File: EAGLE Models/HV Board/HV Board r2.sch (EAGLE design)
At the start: 27 parts, among them K1 HE751, U1 G2RL-1-E, U2 CNY17-3, U3 MJD45H11T4G, U4 MMBT4401-7-F

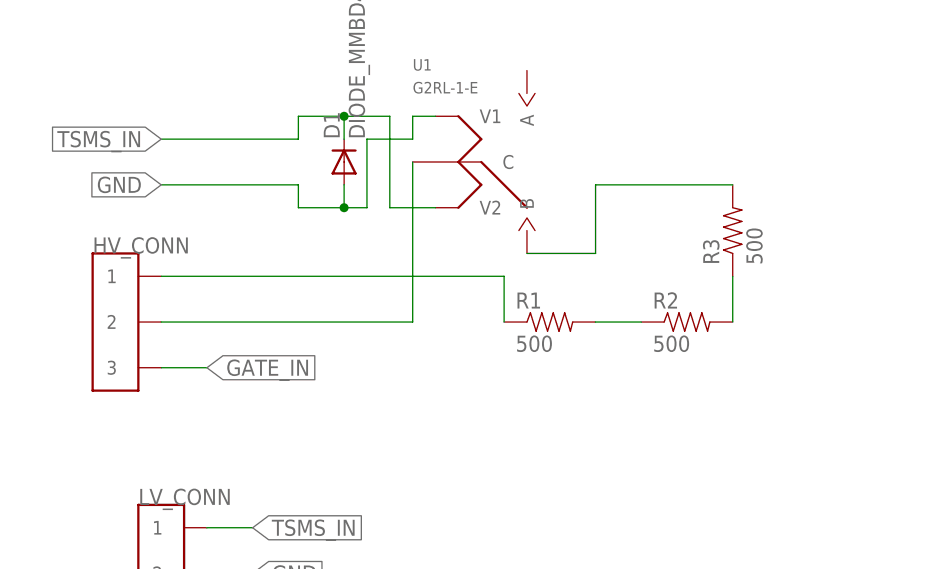
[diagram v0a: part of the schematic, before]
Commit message: Changed HV board for putting in line with MC
Integrated Discharge and TSAL circuit into one smaller board to put in a
box in line with the motor controller.
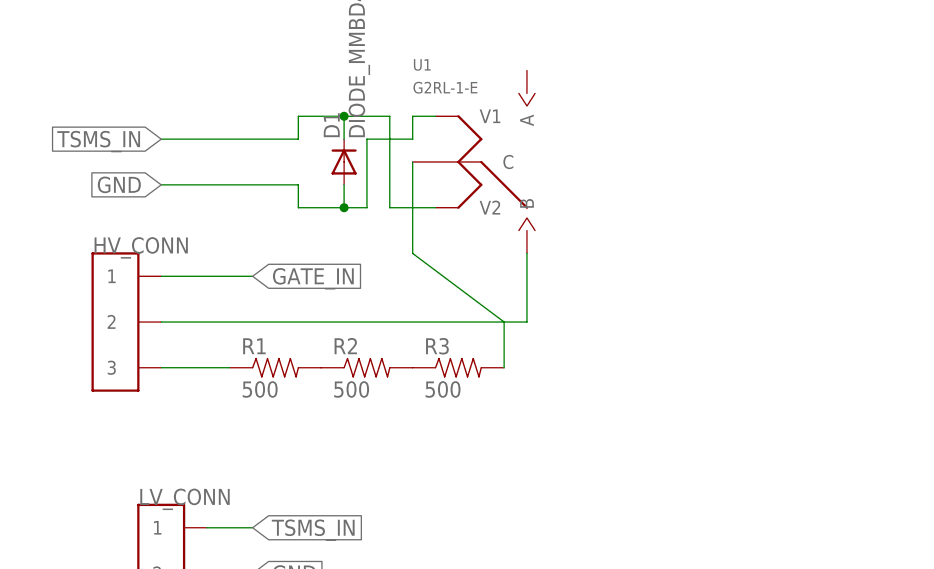
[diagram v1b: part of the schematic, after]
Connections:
- net GATE_IN: now also HV_CONN.1; no longer HV_CONN.3
- net HV+: now also U1.B; no longer U1.C
- net HV-: now also HV_CONN.3; no longer HV_CONN.1
- net N$3: now also U1.C; no longer U1.B
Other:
- moved on the sheet: R1, R2, R3
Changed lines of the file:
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@@
 <?xml version="1.0" encoding="utf-8"?>
 <!DOCTYPE eagle SYSTEM "eagle.dtd">
-<eagle version="7.1.0">
+<eagle version="7.2.0">
 <drawing>
 <settings>
@@
 <instance part="U1" gate="G$1" x="-33.02" y="-91.44"/>
 <instance part="D1" gate="G$1" x="-45.72" y="-91.44" rot="R90"/>
-<instance part="R1" gate="G$1" x="-22.86" y="-109.22"/>
-<instance part="R2" gate="G$1" x="-7.62" y="-109.22"/>
-<instance part="R3" gate="G$1" x="-2.54" y="-99.06" rot="R90"/>
+<instance part="R1" gate="G$1" x="-53.34" y="-114.3"/>
+<instance part="R2" gate="G$1" x="-43.18" y="-114.3"/>
+<instance part="R3" gate="G$1" x="-33.02" y="-114.3"/>
 <instance part="C2" gate="G$1" x="330.2" y="-104.14" smashed="yes">
 <attribute name="NAME" x="334.01" y="-105.41" size="1.778" layer="95" align="center-left"/>
@@
 <net name="N$3" class="0">
 <segment>
-<pinref part="U1" gate="G$1" pin="B"/>
-<wire x1="-25.4" y1="-101.6" x2="-17.78" y2="-101.6" width="0.1524" layer="91"/>
 <pinref part="R3" gate="G$1" pin="2"/>
-<wire x1="-2.54" y1="-93.98" x2="-17.78" y2="-93.98" width="0.1524" layer="91"/>
-<wire x1="-17.78" y1="-93.98" x2="-17.78" y2="-101.6" width="0.1524" layer="91"/>
+<wire x1="-27.94" y1="-114.3" x2="-27.94" y2="-109.22" width="0.1524" layer="91"/>
+<wire x1="-27.94" y1="-109.22" x2="-38.1" y2="-101.6" width="0.1524" layer="91"/>
+<pinref part="U1" gate="G$1" pin="C"/>
+<wire x1="-38.1" y1="-101.6" x2="-38.1" y2="-91.44" width="0.1524" layer="91"/>
 </segment>
 </net>
@@
 <pinref part="R1" gate="G$1" pin="2"/>
 <pinref part="R2" gate="G$1" pin="1"/>
-<wire x1="-17.78" y1="-109.22" x2="-12.7" y2="-109.22" width="0.1524" layer="91"/>
 </segment>
 </net>
@@
 <pinref part="R2" gate="G$1" pin="2"/>
 <pinref part="R3" gate="G$1" pin="1"/>
-<wire x1="-2.54" y1="-109.22" x2="-2.54" y2="-104.14" width="0.1524" layer="91"/>
 </segment>
 </net>
@@
 </segment>
 <segment>
-<pinref part="U1" gate="G$1" pin="C"/>
-<wire x1="-38.1" y1="-109.22" x2="-38.1" y2="-91.44" width="0.1524" layer="91"/>
 <pinref part="HV_CONN" gate="G$1" pin="2"/>
-<wire x1="-66.04" y1="-109.22" x2="-38.1" y2="-109.22" width="0.1524" layer="91"/>
+<wire x1="-25.4" y1="-109.22" x2="-66.04" y2="-109.22" width="0.1524" layer="91"/>
+<pinref part="U1" gate="G$1" pin="B"/>
+<wire x1="-25.4" y1="-109.22" x2="-25.4" y2="-101.6" width="0.1524" layer="91"/>
 </segment>
 </net>
@@
 </segment>
 <segment>
-<pinref part="HV_CONN" gate="G$1" pin="1"/>
-<wire x1="-27.94" y1="-104.14" x2="-66.04" y2="-104.14" width="0.1524" layer="91"/>
 <pinref part="R1" gate="G$1" pin="1"/>
-<wire x1="-27.94" y1="-104.14" x2="-27.94" y2="-109.22" width="0.1524" layer="91"/>
+<pinref part="HV_CONN" gate="G$1" pin="3"/>
+<wire x1="-58.42" y1="-114.3" x2="-66.04" y2="-114.3" width="0.1524" layer="91"/>
 </segment>
 <segment>
@@
 <net name="GATE_IN" class="0">
 <segment>
-<pinref part="HV_CONN" gate="G$1" pin="3"/>
-<wire x1="-66.04" y1="-114.3" x2="-60.96" y2="-114.3" width="0.1524" layer="91"/>
-<label x="-60.96" y="-114.3" size="1.778" layer="95" xref="yes"/>
-</segment>
-<segment>
+<label x="-55.88" y="-104.14" size="1.778" layer="95" xref="yes"/>
+<pinref part="HV_CONN" gate="G$1" pin="1"/>
+<wire x1="-55.88" y1="-104.14" x2="-66.04" y2="-104.14" width="0.1524" layer="91"/>
+</segment>
+<segment>
